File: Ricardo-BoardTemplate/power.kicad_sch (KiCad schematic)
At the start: 23 parts, among them U3 LM66100, U4 LM66100, U5 MAX77827AEFD+T, U6 SC4215

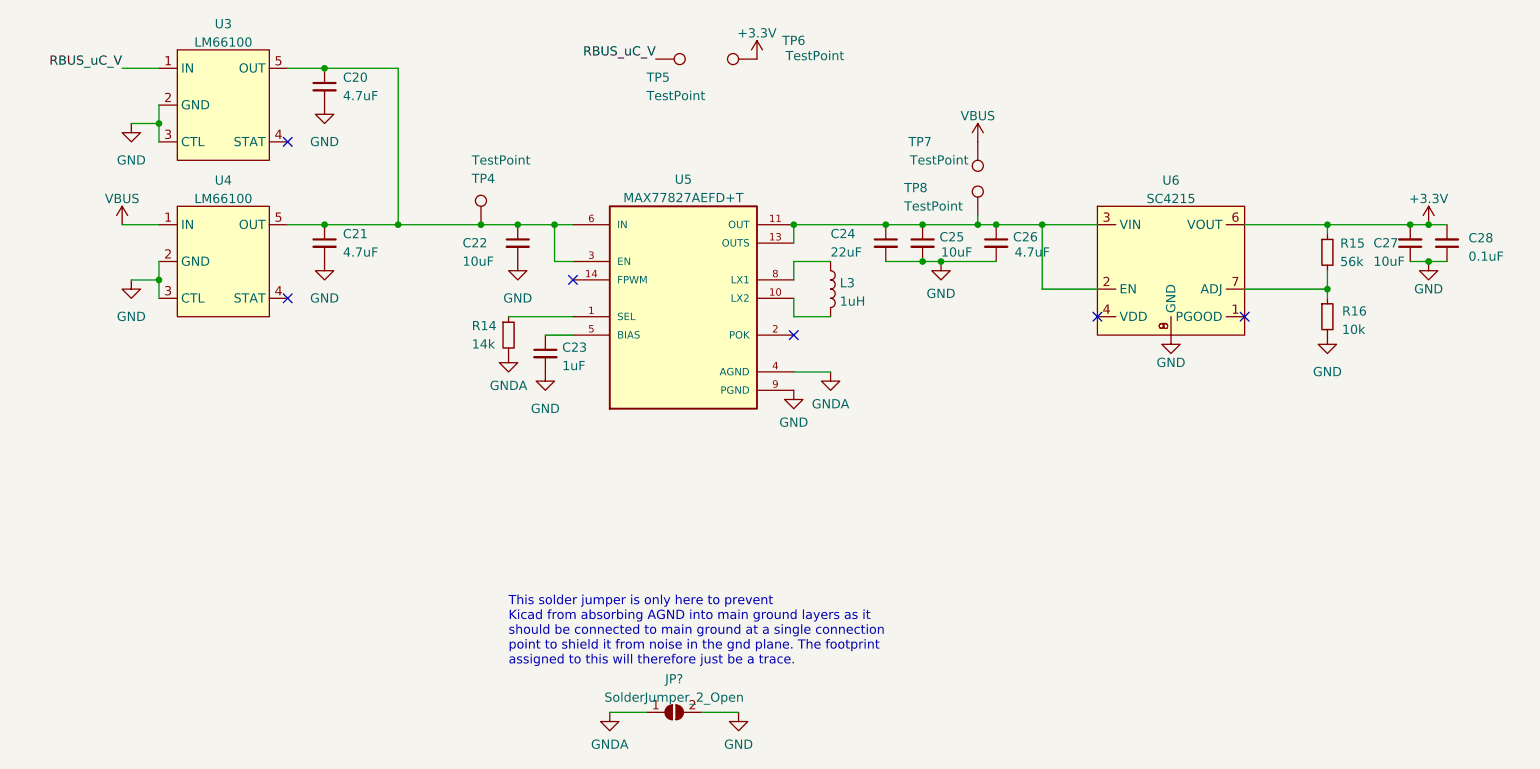
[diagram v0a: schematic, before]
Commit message: Initial buck boost layout
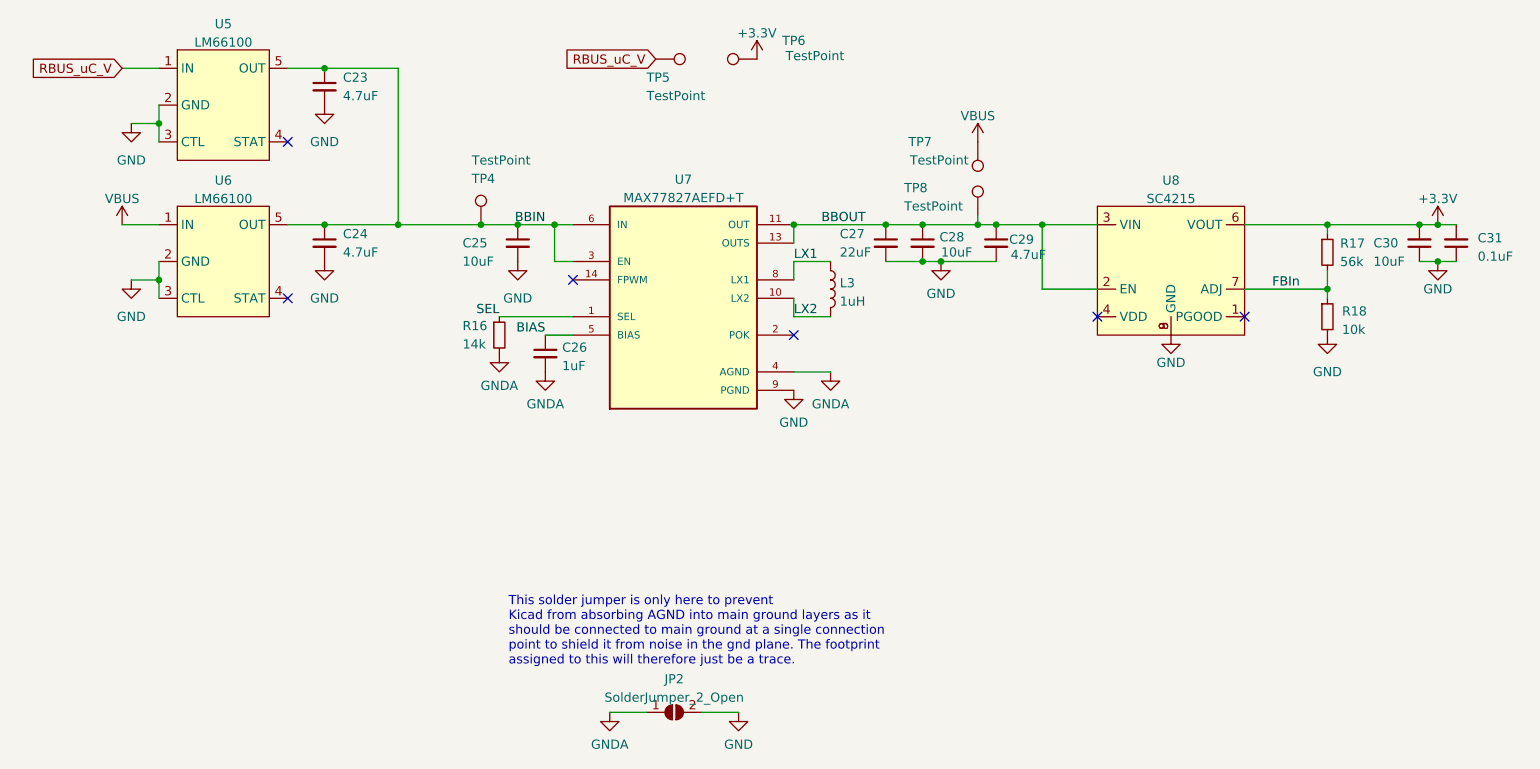
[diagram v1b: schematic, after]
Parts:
- C25: renamed from C22; footprint Capacitor_SMD:C_0402_1005Metric -> Capacitor_SMD:C_0603_1608Metric
- C30: renamed from C27; footprint Capacitor_SMD:C_0603_1608Metric -> Capacitor_SMD:C_0402_1005Metric
- C31: renamed from C28; footprint Capacitor_SMD:C_0603_1608Metric -> Capacitor_SMD:C_0402_1005Metric
- R17: renamed from R15; footprint Resistor_SMD:R_0603_1608Metric -> Resistor_SMD:R_0402_1005Metric
- R18: renamed from R16; footprint Resistor_SMD:R_0603_1608Metric -> Resistor_SMD:R_0402_1005Metric
- gave numbers to parts that had none: 1
- renumbered C20 to C23, C21 to C24, C23 to C26, C24 to C27, C25 to C28, C26 to C29, R14 to R16, U3 to U5, U4 to U6, U5 to U7, U6 to U8
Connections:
- net GND: no longer C26.2
- net GNDA: now also C26.2
- net BBOUT: now reaches C27.1, C28.1, C29.1, TP8.1, U7.11 (OUT), U7.13 (OUTS), U8.2 (EN), U8.3 (VIN)
- net SEL: now reaches R16.1, U7.1 (SEL)
- net LX1: now reaches L3.1, U7.8 (LX1)
- net LX2: now reaches L3.2, U7.10 (LX2)
- net BBIN: now reaches C23.1, C24.1, C25.1, TP4.1, U5.5 (OUT), U6.5 (OUT), U7.3 (EN), U7.6 (IN)
- net FBIn: now reaches R17.2, R18.1, U8.7 (ADJ)
- net BIAS: now reaches C26.1, U7.5 (BIAS)
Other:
- moved on the sheet: C30, C31, R16
